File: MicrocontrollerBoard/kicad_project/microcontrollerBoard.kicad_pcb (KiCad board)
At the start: 2 copper layers, 78.7 x 63.5 mm, 58 parts, among them J1 PROG_CONN, J10 PC_5V, J11 CONN_RESET, J13 PA_GND, J14 PB_GND, J15 PC_GND, J18 COM, J19 COM_5V, J2 5V_CONN, J20 COM_GND, J21 POWER_CONN, J22 MOTOR2, J23 MOTOR1, J3 PA, J4 PB, J5 PC, J6 3V_CONN_1, J7 3V_CONN_2, J8 PA_5V, J9 PB_5V, U1 ATmega1284P-PU, U2 TC4422, U3 TC4422, U4 TC4422, U5 TC4422, U6 AMS1117-3.3, Y1 16MHz

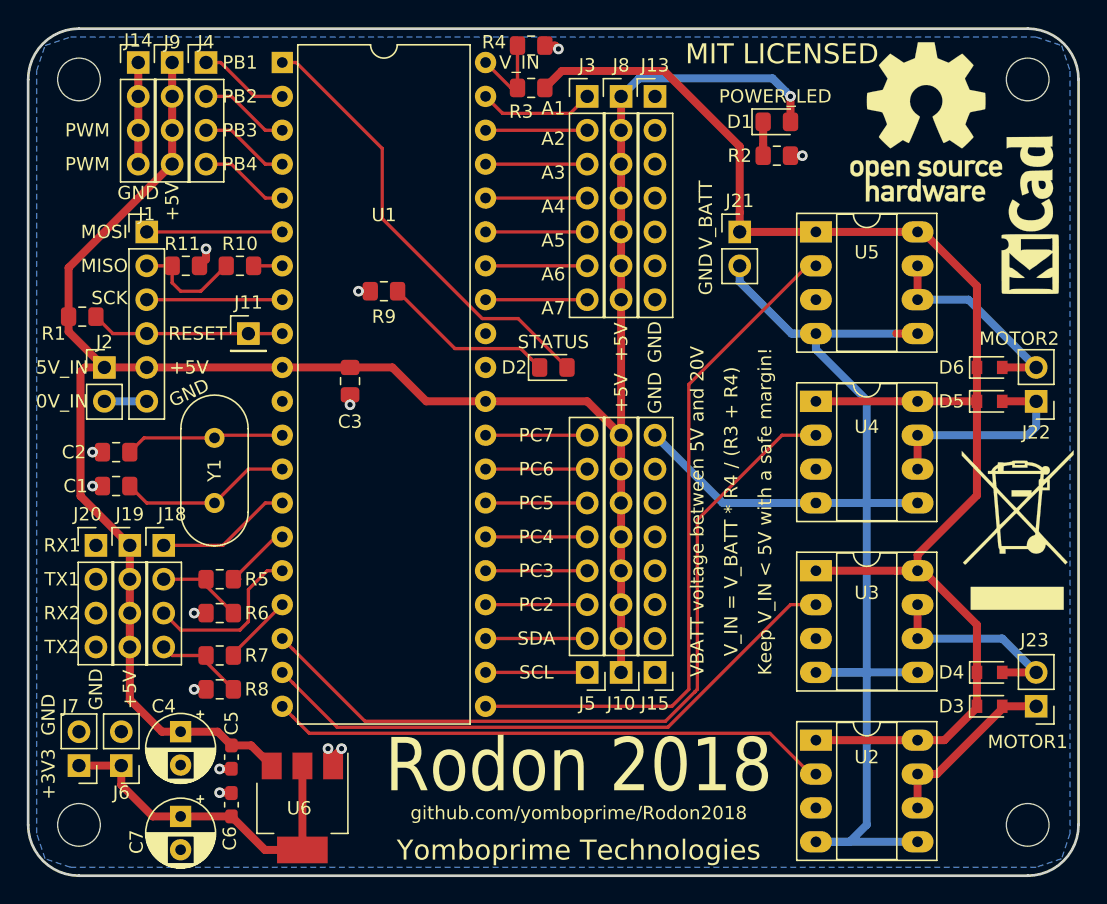
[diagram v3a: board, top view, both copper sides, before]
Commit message: Revised ICSP header, motor diodes.
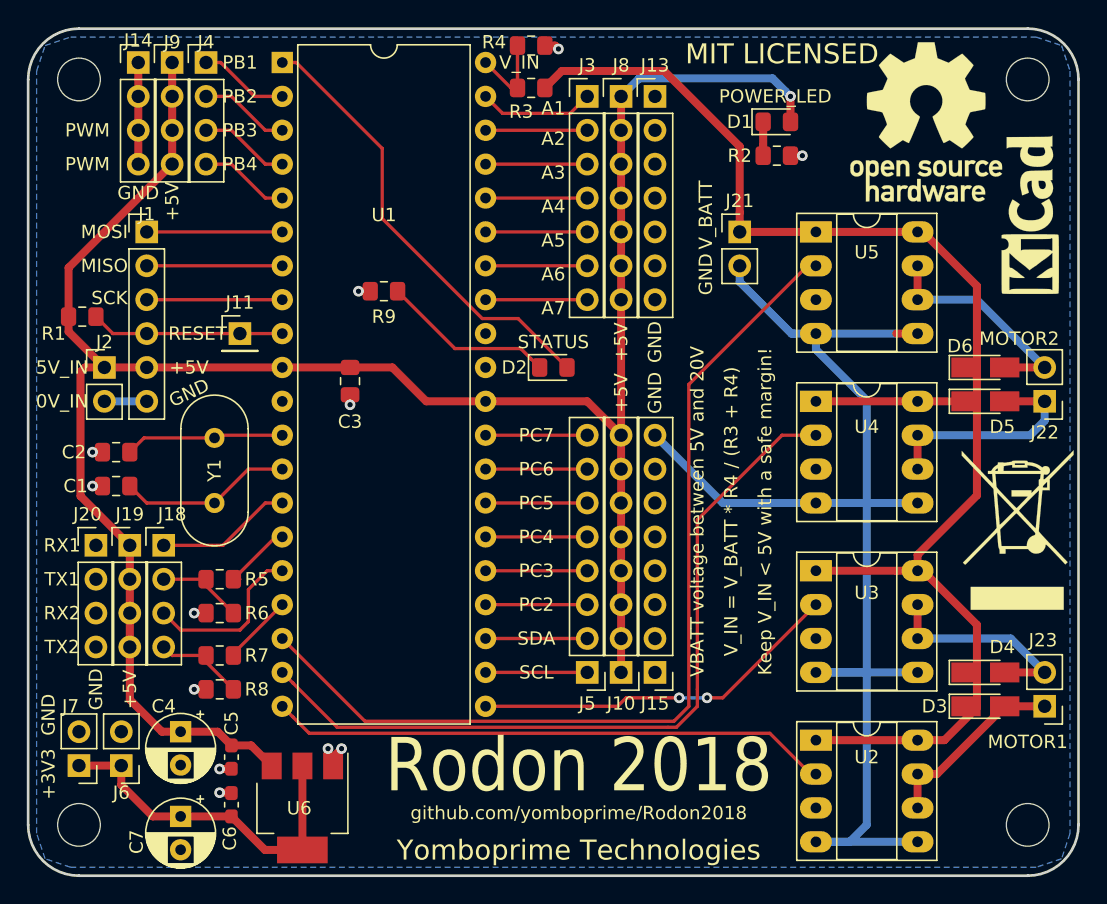
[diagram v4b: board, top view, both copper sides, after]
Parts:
- removed R10: 1K, Resistor_SMD:R_0805_2012Metric_Pad1.15x1.40mm_HandSolder
- removed R11: 2K, Resistor_SMD:R_0805_2012Metric_Pad1.15x1.40mm_HandSolder
- D3, D4, D5, D6: footprint Diode_SMD:D_SOD-110 -> Diode_SMD:D_MicroMELF_Hadsoldering
- moved J11 0.63 mm to (90.8, 73.7)
- moved J22 0.63 mm to (151.1, 78.7)
- moved J23 0.63 mm to (151.1, 101.6)
- moved D3 0.32 mm to (146.7, 101.6)
- moved D4 0.32 mm to (146.7, 99.1)
- moved D5 0.32 mm to (146.7, 78.7)
- moved D6 0.32 mm to (146.7, 76.2)
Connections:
- J1 pad 2: Net-(J1-Pad2) -> MISO
- U1 pad 18: MOTOR2A -> MOTOR2B
- U1 pad 19: MOTOR1B -> MOTOR2A
- U1 pad 21: MOTOR2B -> MOTOR1B
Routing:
- net MOTOR2B: track 51.8 -> 70.9 mm
- net MOTOR1B: track 45.5 -> 27.9 mm, vias 0 -> 2
- net Net-(J1-Pad2): track 8.28 -> 0.00 mm
- net MISO: track 2.15 -> 10.2 mm
- net GND: track 128.1 -> 126.6 mm, vias 13 -> 12
- net Net-(D6-Pad2): track 16.1 -> 17.2 mm
- net Net-(D4-Pad2): track 15.0 -> 16.1 mm
- net Net-(D5-Pad2): track 16.1 -> 17.0 mm

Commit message: uC board: Add motor diodes values (LL4148)
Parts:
- D3, D4, D5, D6: value D -> LL4148
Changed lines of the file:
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@@
       (effects (font (size 1 1) (thickness 0.15)))
     )
-    (fp_text value D (at 0 1.55) (layer F.Fab)
+    (fp_text value LL4148 (at 0 1.55) (layer F.Fab)
       (effects (font (size 1 1) (thickness 0.15)))
     )
@@
       (effects (font (size 1 1) (thickness 0.15)))
     )
-    (fp_text value D (at 0 1.55) (layer F.Fab)
+    (fp_text value LL4148 (at 0 1.55) (layer F.Fab)
       (effects (font (size 1 1) (thickness 0.15)))
     )
@@
       (effects (font (size 1 1) (thickness 0.15)))
     )
-    (fp_text value D (at 0 1.55) (layer F.Fab)
+    (fp_text value LL4148 (at 0 1.55) (layer F.Fab)
       (effects (font (size 1 1) (thickness 0.15)))
     )
@@
       (effects (font (size 1 1) (thickness 0.15)))
     )
-    (fp_text value D (at 0 1.55) (layer F.Fab)
+    (fp_text value LL4148 (at 0 1.55) (layer F.Fab)
       (effects (font (size 1 1) (thickness 0.15)))
     )
